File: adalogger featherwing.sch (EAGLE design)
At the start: 18 parts, among them IC1 RTC_PCF8523T, SW1 KMR2, X4 microsd, Y1 32khz

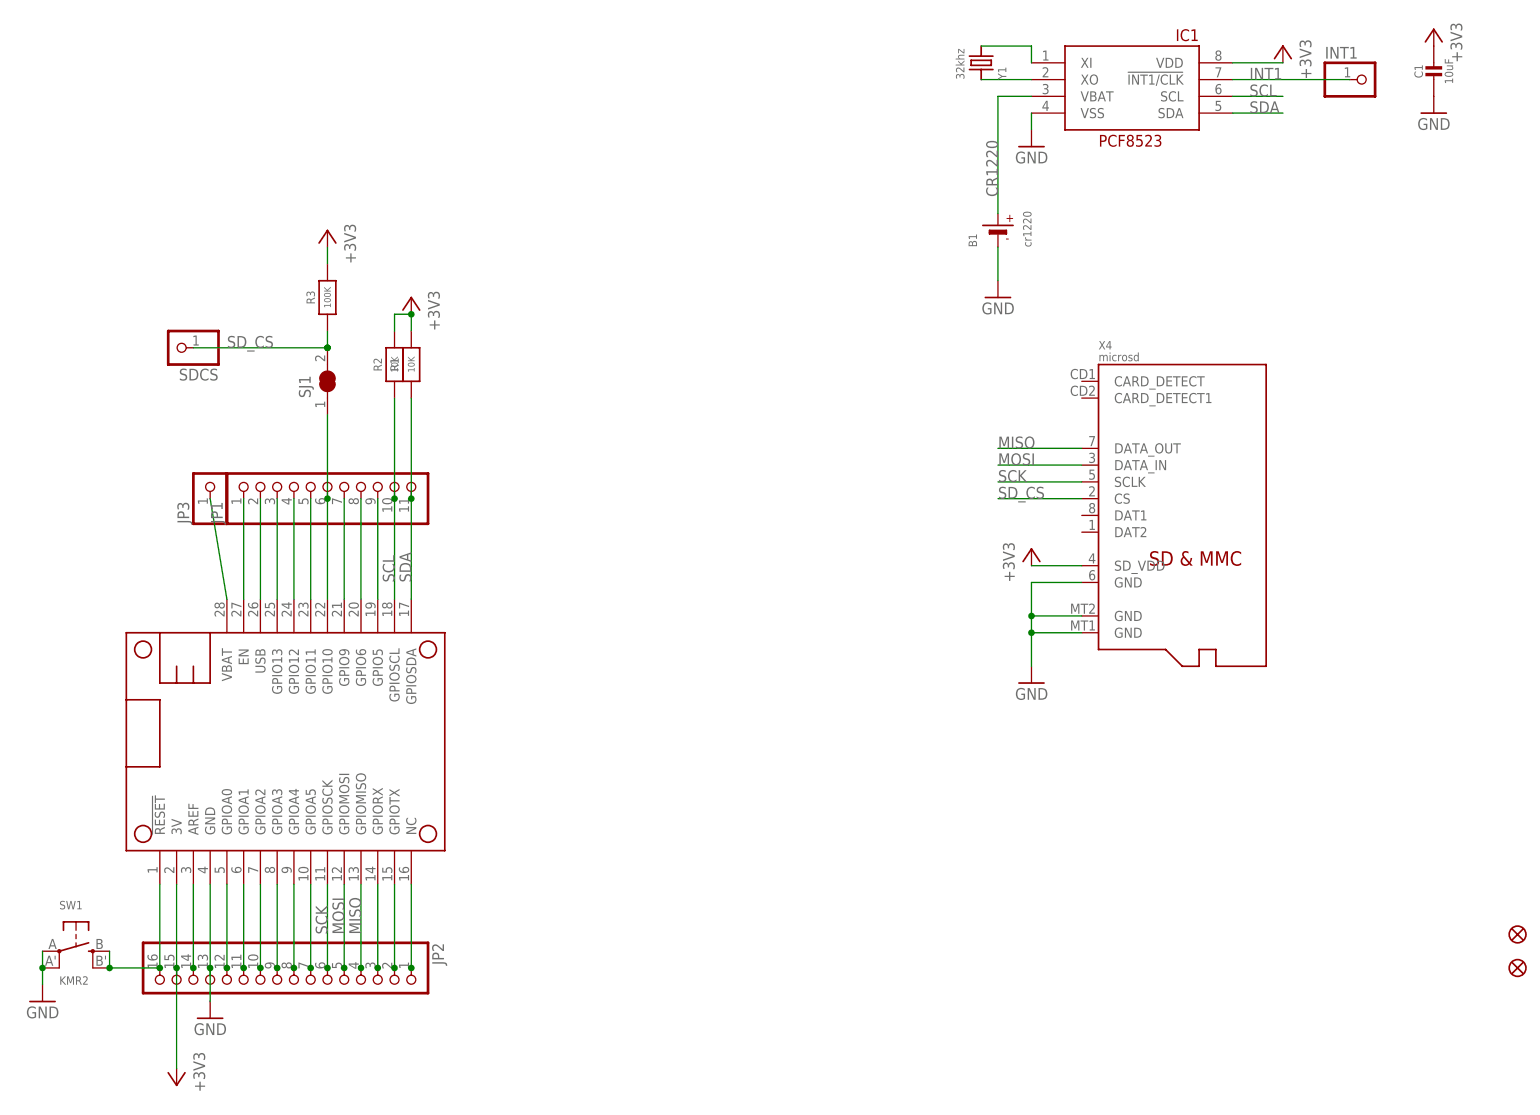
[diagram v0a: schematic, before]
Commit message: update with RC filter
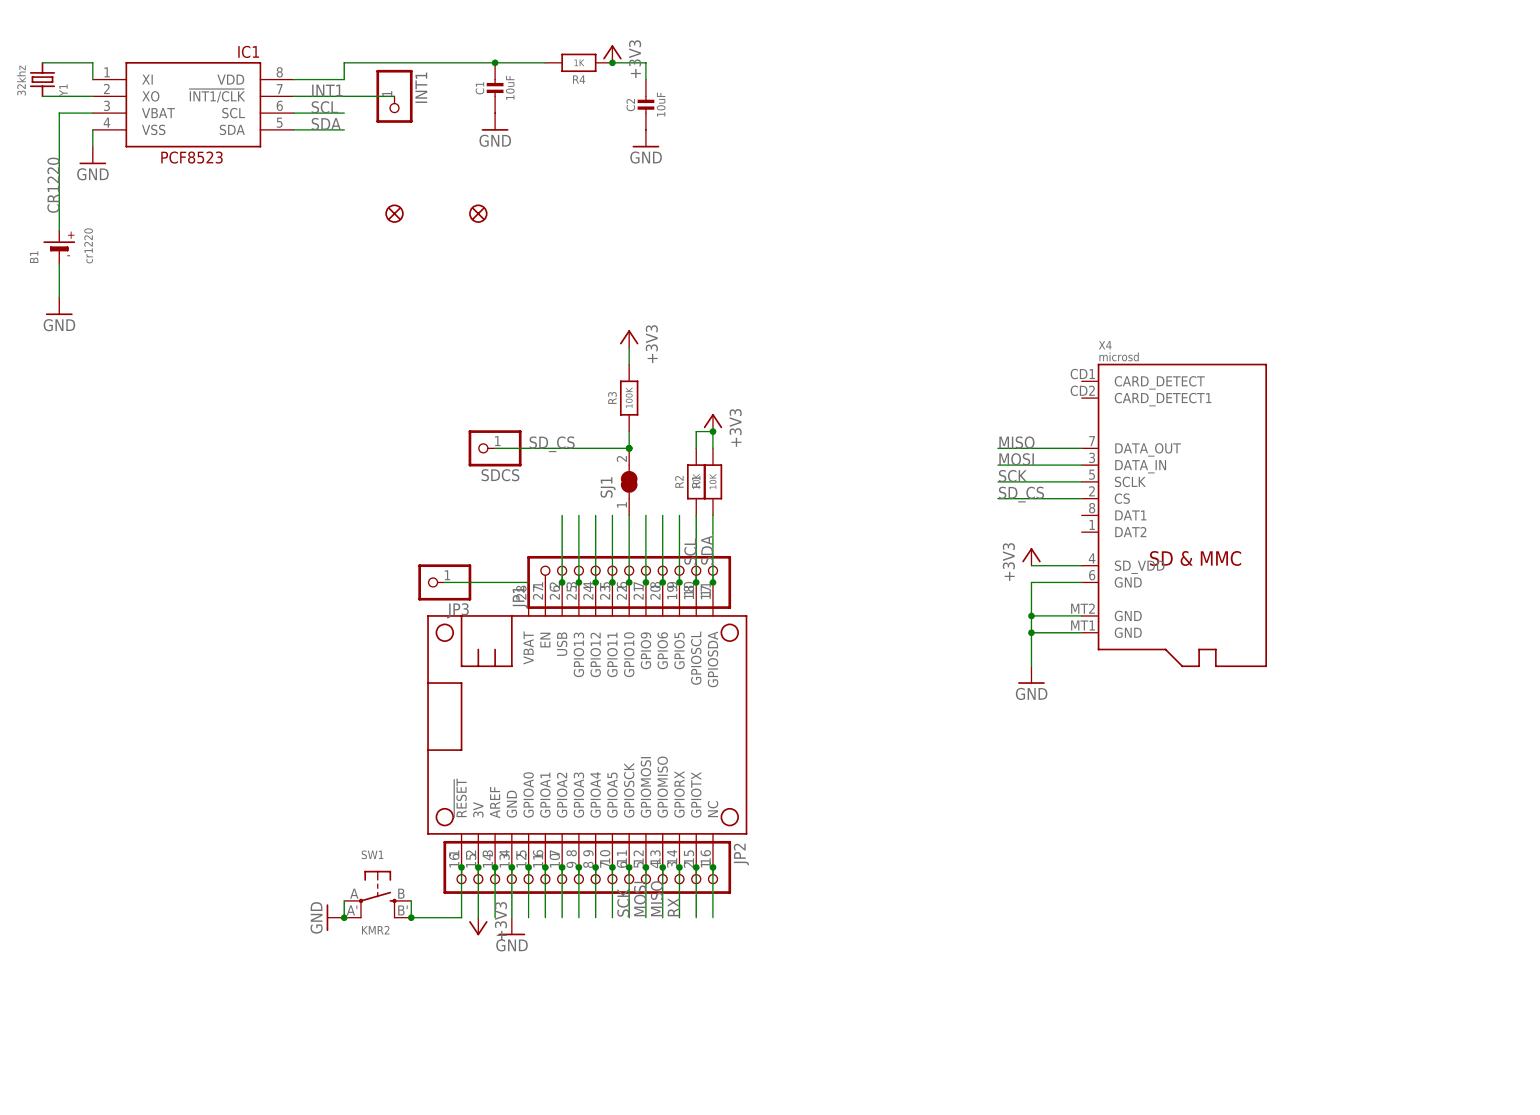
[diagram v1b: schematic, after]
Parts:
- added C2: 10uF, microbuilder:CAP_CERAMIC0805-NOOUTLINE
- added R4: 1K, microbuilder:RESISTOR_0603_NOOUT
- FID1, FID2: value FIDUCIAL"" -> FIDUCIAL_1MM; device microbuilder:FIDUCIAL"" -> microbuilder:FIDUCIAL_1MM
- IC1: value RTC_PCF8523T -> PCF8523T
- R1, R2, R3: device microbuilder:RESISTOR0805_NOOUTLINE -> microbuilder:RESISTOR_0603_NOOUT
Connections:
- net D10 renamed CS
- net N$1 renamed RESET
- net N$10 renamed F
- net N$11 renamed E
- net N$12 renamed D
- net N$13 renamed C
- net N$14 renamed B
- net N$15 renamed A
- net N$16 renamed EN
- net N$17 renamed AREF
- net N$19 renamed L
- net N$2 renamed G
- net N$21 renamed J
- net N$22 renamed I
- net N$23 renamed H
- net N$3 renamed N
- net N$4 renamed TX
- net N$5 renamed M
- net N$6 renamed RX
- new net N$1: C1.1, IC1.VDD, R4.2
- net +3V3: now also C2.1, R4.1; no longer C1.1, IC1.VDD
- net GND: now also C2.2
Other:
- moved on the sheet: B1, C1, IC1, INT1, JP1, JP2, JP3, R1, R2, R3, SDCS, SJ1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
